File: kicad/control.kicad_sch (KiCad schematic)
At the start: 14 parts, among them U10 74LS08, U11 74LS138, U2 74LS112, U8 74LS00, U9 74LS00

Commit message: updates to start v1 rev2, pcb layout updates
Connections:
- net A14: now also U10.12, U11.4 (E1); no longer U11.5 (E2), U8.9
- net A15: now also U10.13; no longer U8.10
- net GND: now also U8.10, U8.9; no longer U10.12, U10.13
- net PHI2: now also U10.1, U9.1; no longer U10.2, U9.2
- net ROM_ACC: now also U9.10; no longer U9.9
- net ROM_AD: now also U10.11, U10.2; no longer U10.1, U8.8
- net ~{A15}: now also U11.5 (E2), U9.2; no longer U11.4 (E1), U9.1
- net ~{ROM_SEL}: now also U9.9; no longer U9.10
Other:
- moved on the sheet: U10C, U10D, U8A, U8C
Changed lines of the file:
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@@
 		(title "6502 ATTY1")
 		(date "2025-12-16")
-		(rev "1")
+		(rev "2")
 		(comment 1 "© 2025 Ben Dooks")
 	)
@@
 	)
 	(junction
-		(at 44.45 140.97)
+		(at 44.45 137.16)
 		(diameter 0)
 		(color 0 0 0 0)
@@
 	(wire
 		(pts
+			(xy 43.18 77.47) (xy 52.07 77.47)
+		)
+		(stroke
+			(width 0)
+			(type default)
+		)
+	)
+	(wire
+		(pts
 			(xy 43.18 72.39) (xy 52.07 72.39)
 		)
@@
 	(wire
 		(pts
-			(xy 62.23 140.97) (xy 72.39 140.97)
+			(xy 62.23 137.16) (xy 72.39 137.16)
 		)
 		(stroke
@@
 	(wire
 		(pts
-			(xy 44.45 138.43) (xy 44.45 140.97)
+			(xy 44.45 134.62) (xy 44.45 137.16)
 		)
 		(stroke
@@
 	(wire
 		(pts
-			(xy 38.1 140.97) (xy 44.45 140.97)
+			(xy 38.1 137.16) (xy 44.45 137.16)
 		)
 		(stroke
@@
 	(wire
 		(pts
-			(xy 44.45 143.51) (xy 46.99 143.51)
+			(xy 44.45 139.7) (xy 46.99 139.7)
 		)
 		(stroke
@@
 	(wire
 		(pts
-			(xy 44.45 140.97) (xy 44.45 143.51)
+			(xy 44.45 137.16) (xy 44.45 139.7)
 		)
 		(stroke
@@
 	(wire
 		(pts
-			(xy 46.99 138.43) (xy 44.45 138.43)
+			(xy 46.99 134.62) (xy 44.45 134.62)
 		)
 		(stroke
@@
 	(wire
 		(pts
-			(xy 43.18 74.93) (xy 52.07 74.93)
-		)
-		(stroke
-			(width 0)
-			(type default)
-		)
-	)
-	(wire
-		(pts
 			(xy 261.62 140.97) (xy 261.62 143.51)
 		)
@@
 	(wire
 		(pts
-			(xy 43.18 77.47) (xy 52.07 77.47)
+			(xy 45.72 74.93) (xy 52.07 74.93)
 		)
 		(stroke
@@
 	)
 	(label "~{R}W"
-		(at 69.85 140.97 180)
+		(at 69.85 137.16 180)
 		(effects
 			(font
@@
 	)
 	(label "~{A15}"
-		(at 43.18 77.47 0)
+		(at 45.72 74.93 0)
 		(effects
 			(font
@@
 	(hierarchical_label "A14"
 		(shape input)
-		(at 43.18 74.93 180)
+		(at 43.18 77.47 180)
 		(effects
 			(font
@@
 	(hierarchical_label "R~{W}"
 		(shape input)
-		(at 38.1 140.97 180)
+		(at 38.1 137.16 180)
 		(effects
 			(font
@@
 	(hierarchical_label "~{R}W"
 		(shape output)
-		(at 72.39 140.97 0)
+		(at 72.39 137.16 0)
 		(effects
 			(font
@@
 		(lib_id "74xx:74LS00")
 		(at 184.15 132.08 0)
+		(mirror x)
 		(unit 3)
 		(exclude_from_sim no)
@@
 		(on_board yes)
 		(dnp no)
-		(fields_autoplaced yes)
 		(property "Reference" "U9"
-			(at 184.1417 123.19 0)
+			(at 183.896 124.206 0)
 			(effects
 				(font
@@
 		)
 		(property "Value" "74LS00"
-			(at 184.1417 125.73 0)
+			(at 184.15 126.238 0)
 			(effects
 				(font
@@
 		(lib_id "74xx:74LS00")
 		(at 66.04 31.75 0)
+		(mirror x)
 		(unit 1)
 		(exclude_from_sim no)
@@
 		(on_board yes)
 		(dnp no)
-		(fields_autoplaced yes)
 		(property "Reference" "U9"
-			(at 66.0317 22.86 0)
+			(at 65.532 24.384 0)
 			(effects
 				(font
@@
 		)
 		(property "Value" "74LS00"
-			(at 66.0317 25.4 0)
+			(at 65.532 26.416 0)
 			(effects
 				(font
@@
 	(symbol
 		(lib_id "74xx:74LS00")
-		(at 119.38 97.79 0)
+		(at 271.78 138.43 0)
 		(unit 3)
 		(exclude_from_sim no)
@@
 		(fields_autoplaced yes)
 		(property "Reference" "U8"
-			(at 119.3717 88.9 0)
+			(at 271.7717 129.54 0)
 			(effects
 				(font
@@
 		)
 		(property "Value" "74LS00"
-			(at 119.3717 91.44 0)
+			(at 271.7717 132.08 0)
 			(effects
 				(font
@@
 		)
 		(property "Footprint" "Package_DIP:DIP-14_W7.62mm"
-			(at 119.38 97.79 0)
+			(at 271.78 138.43 0)
 			(effects
 				(font
@@
 		)
 		(property "Datasheet" "http://www.ti.com/lit/gpn/sn74ls00"
-			(at 119.38 97.79 0)
+			(at 271.78 138.43 0)
 			(effects
 				(font
@@
 		)
 		(property "Description" "quad 2-input NAND gate"
-			(at 119.38 97.79 0)
+			(at 271.78 138.43 0)
 			(effects
 				(font
@@
 	(symbol
 		(lib_id "74xx:74LS00")
-		(at 54.61 140.97 0)
+		(at 54.61 137.16 0)
 		(unit 1)
 		(exclude_from_sim no)
@@
 		(fields_autoplaced yes)
 		(property "Reference" "U8"
-			(at 54.6017 132.08 0)
+			(at 54.6017 128.27 0)
 			(effects
 				(font
@@
 		)
 		(property "Value" "74LS00"
-			(at 54.6017 134.62 0)
+			(at 54.6017 130.81 0)
 			(effects
 				(font
@@
 		)
 		(property "Footprint" "Package_DIP:DIP-14_W7.62mm"
-			(at 54.61 140.97 0)
+			(at 54.61 137.16 0)
 			(effects
 				(font
@@
 		)
 		(property "Datasheet" "http://www.ti.com/lit/gpn/sn74ls00"
-			(at 54.61 140.97 0)
+			(at 54.61 137.16 0)
 			(effects
 				(font
@@
 		)
 		(property "Description" "quad 2-input NAND gate"
-			(at 54.61 140.97 0)
+			(at 54.61 137.16 0)
 			(effects
 				(font
@@
 		(lib_id "74xx:74LS08")
 		(at 140.97 111.76 0)
+		(mirror x)
 		(unit 1)
 		(exclude_from_sim no)
@@
 		(dnp no)
 		(property "Reference" "U10"
-			(at 140.9617 102.87 0)
+			(at 139.954 103.886 0)
 			(effects
 				(font
@@
 		)
 		(property "Value" "74LS08"
-			(at 140.9617 105.41 0)
+			(at 140.462 105.918 0)
 			(effects
 				(font
@@
 	(symbol
 		(lib_id "74xx:74LS08")
-		(at 271.78 138.43 0)
+		(at 270.51 118.11 0)
 		(unit 3)
 		(exclude_from_sim no)
@@
 		(fields_autoplaced yes)
 		(property "Reference" "U10"
-			(at 271.7717 129.54 0)
+			(at 270.5017 109.22 0)
 			(effects
 				(font
@@
 		)
 		(property "Value" "74LS08"
-			(at 271.7717 132.08 0)
+			(at 270.5017 111.76 0)
 			(effects
 				(font
@@
 		)
 		(property "Footprint" "Package_DIP:DIP-14_W7.62mm"
-			(at 271.78 138.43 0)
+			(at 270.51 118.11 0)
 			(effects
 				(font
@@
 		)
 		(property "Datasheet" "http://www.ti.com/lit/gpn/sn74LS08"
-			(at 271.78 138.43 0)
+			(at 270.51 118.11 0)
 			(effects
 				(font
@@
 		)
 		(property "Description" "Quad And2"
-			(at 271.78 138.43 0)
+			(at 270.51 118.11 0)
 			(effects
 				(font
@@
 	(symbol
 		(lib_id "74xx:74LS08")
-		(at 270.51 118.11 0)
+		(at 119.38 97.79 0)
 		(unit 4)
 		(exclude_from_sim no)
@@
 		(fields_autoplaced yes)
 		(property "Reference" "U10"
-			(at 270.5017 109.22 0)
+			(at 119.3717 88.9 0)
 			(effects
 				(font
@@
 		)
 		(property "Value" "74LS08"
-			(at 270.5017 111.76 0)
+			(at 119.3717 91.44 0)
 			(effects
 				(font
@@
 		)
 		(property "Footprint" "Package_DIP:DIP-14_W7.62mm"
-			(at 270.51 118.11 0)
+			(at 119.38 97.79 0)
 			(effects
 				(font
@@
 		)
 		(property "Datasheet" "http://www.ti.com/lit/gpn/sn74LS08"
-			(at 270.51 118.11 0)
+			(at 119.38 97.79 0)
 			(effects
 				(font
@@
 		)
 		(property "Description" "Quad And2"
-			(at 270.51 118.11 0)
+			(at 119.38 97.79 0)
 			(effects
 				(font

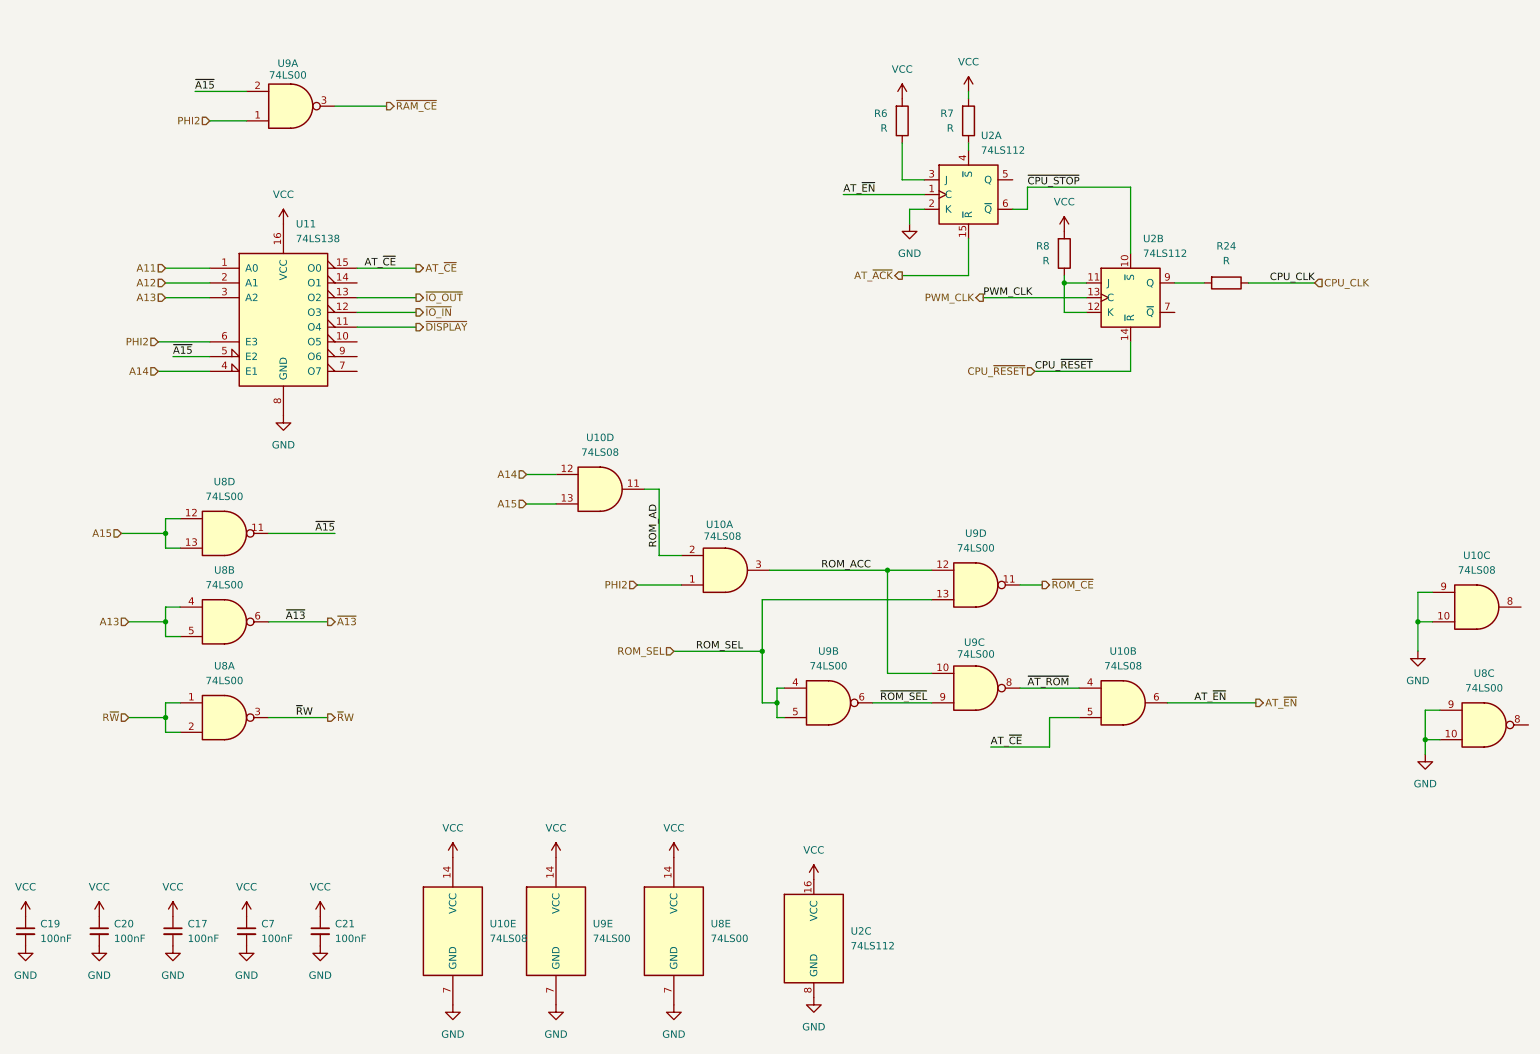
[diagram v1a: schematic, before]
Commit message: value updates, fix ROM ~WE
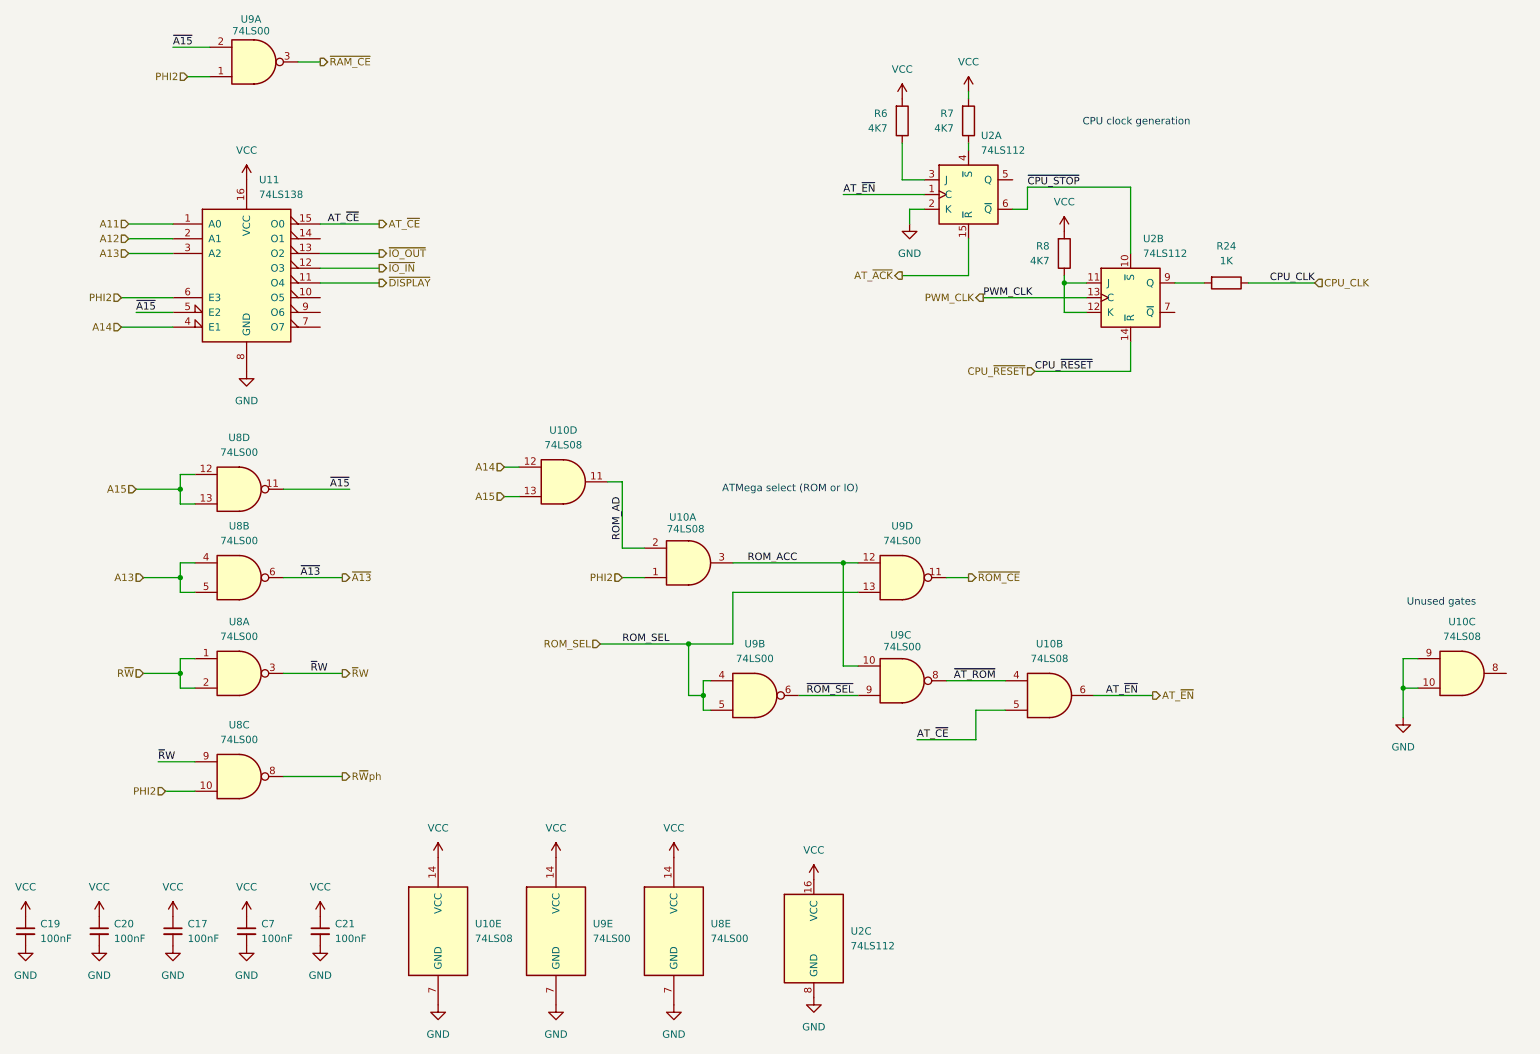
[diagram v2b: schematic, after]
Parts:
- R24: value R -> 1K
- R6, R7, R8: value R -> 4K7
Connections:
- net GND: no longer U8.10, U8.9
- net PHI2: now also U8.10
- net ~{R}W: now also U8.9
- net R~{W}ph: now reaches U8.8
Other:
- note added: "ATMega select (ROM or IO)"
- note added: "CPU clock generation"
- note added: "Unused gates"
- moved on the sheet: U10A, U10B, U10C, U10D, U10E, U11, U8A, U8B, U8C, U8D, U9A, U9B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

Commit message: more updates for v1 rev2
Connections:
- net ~{RAM_CE} is gone; now on net ~{A15}: U9.3
- net A15: now also U9.1, U9.2; no longer U8.12, U8.13
- net GND: now also U10.1, U10.2, U8.1, U8.2; no longer U10.10, U10.9
- net PHI2: now also U10.9; no longer U10.1, U9.1
- net ROM_ACC: now also U10.8; no longer U10.3
- net ROM_AD: now also U10.10; no longer U10.2
- net R~{W}: now also U8.12, U8.13; no longer U8.1, U8.2
- net ~{A15}: no longer U8.11, U9.2
- net ~{R}W: now also U8.11; no longer U8.3
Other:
- moved on the sheet: R24, R6, R7, R8, U10A, U10C, U2A, U2B, U8A, U8D, U9A

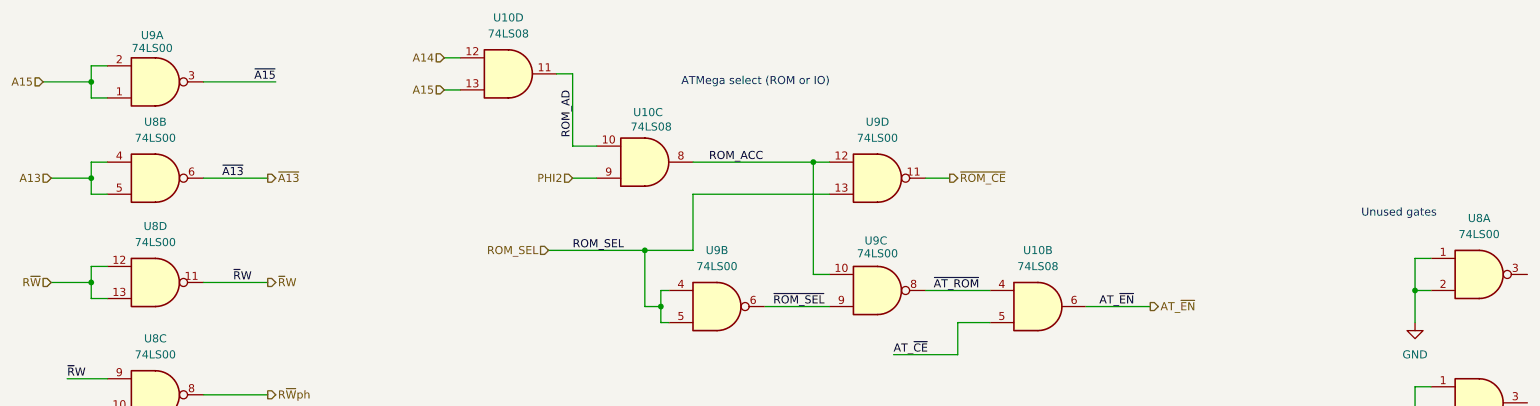
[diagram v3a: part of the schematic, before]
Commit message: pcb updates, remove resistor on xtal, smaller board
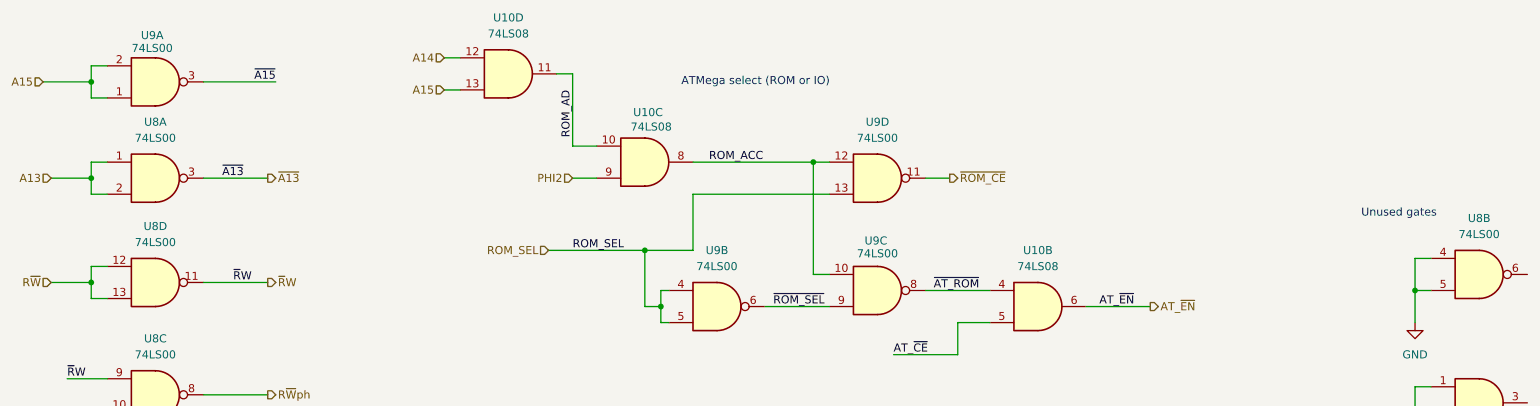
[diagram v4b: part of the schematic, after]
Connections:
- net A13: now also U8.1, U8.2; no longer U8.4, U8.5
- net GND: now also U8.4, U8.5; no longer U8.1, U8.2
- net ~{A13}: now also U8.3; no longer U8.6
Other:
- moved on the sheet: U8A, U8B
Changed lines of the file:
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@@
 	(symbol
 		(lib_id "74xx:74LS00")
-		(at 57.15 113.03 0)
+		(at 266.7 128.27 0)
 		(unit 2)
 		(exclude_from_sim no)
@@
 		(fields_autoplaced yes)
 		(property "Reference" "U8"
-			(at 57.1417 104.14 0)
+			(at 266.6917 119.38 0)
 			(effects
 				(font
@@
 		)
 		(property "Value" "74LS00"
-			(at 57.1417 106.68 0)
+			(at 266.6917 121.92 0)
 			(effects
 				(font
@@
 		)
 		(property "Footprint" "Package_DIP:DIP-14_W7.62mm"
-			(at 57.15 113.03 0)
+			(at 266.7 128.27 0)
 			(effects
 				(font
@@
 		)
 		(property "Datasheet" "http://www.ti.com/lit/gpn/sn74ls00"
-			(at 57.15 113.03 0)
+			(at 266.7 128.27 0)
 			(effects
 				(font
@@
 		)
 		(property "Description" "quad 2-input NAND gate"
-			(at 57.15 113.03 0)
+			(at 266.7 128.27 0)
 			(effects
 				(font
@@
 	(symbol
 		(lib_id "74xx:74LS00")
-		(at 266.7 128.27 0)
+		(at 57.15 113.03 0)
 		(unit 1)
 		(exclude_from_sim no)
@@
 		(fields_autoplaced yes)
 		(property "Reference" "U8"
-			(at 266.6917 119.38 0)
+			(at 57.1417 104.14 0)
 			(effects
 				(font
@@
 		)
 		(property "Value" "74LS00"
-			(at 266.6917 121.92 0)
+			(at 57.1417 106.68 0)
 			(effects
 				(font
@@
 		)
 		(property "Footprint" "Package_DIP:DIP-14_W7.62mm"
-			(at 266.7 128.27 0)
+			(at 57.15 113.03 0)
 			(effects
 				(font
@@
 		)
 		(property "Datasheet" "http://www.ti.com/lit/gpn/sn74ls00"
-			(at 266.7 128.27 0)
+			(at 57.15 113.03 0)
 			(effects
 				(font
@@
 		)
 		(property "Description" "quad 2-input NAND gate"
-			(at 266.7 128.27 0)
+			(at 57.15 113.03 0)
 			(effects
 				(font
